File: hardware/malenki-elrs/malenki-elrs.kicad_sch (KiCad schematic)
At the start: 36 parts, among them J1 Conn_01x02_Male-Connector, J2 PROG Header, J3 Weapons, U1 SPX3819M5-L-3-3, U7 ESP32-S3FN8, Y1 ECS-400-10-37B2-CKY-TR

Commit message: Generated production files
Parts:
- C1, C14, C5: LCSC C96446 -> (none); LCSC Part # (none) -> C96446; Manufacturer Samsung -> (none)
- C10, C11, C13, C4, C7, C9: LCSC C1525 -> (none); LCSC Part # (none) -> C1525
- C12, C15, C8: LCSC C52923 -> (none); LCSC Part # (none) -> C52923
- C2, C3: LCSC C1547 -> (none); LCSC Part # (none) -> C1547
- C6: LCSC C15195 -> (none); LCSC Part # (none) -> C15195
- D2: LCSC C25503345 -> (none); LCSC Part # (none) -> C25503345; Manufacturer XINGLIGHT -> (none)
- L4: LCSC C76884 -> (none); LCSC Part # (none) -> C76884
- R1, R13, R2, R6, R8: LCSC C25744 -> (none); LCSC Part # (none) -> C25744
- R10, R11, R12, R14, R3, R4, R5: LCSC C25117 -> (none); LCSC Part # (none) -> C25117
- R7: LCSC C25779 -> (none); LCSC Part # (none) -> C25779
- U1: LCSC C9055 -> (none); LCSC Part # (none) -> C9055
- U2: renamed from U7; LCSC C2913196 -> (none); LCSC Part # (none) -> C2913196
- Y1: LCSC C5371760 -> (none); LCSC Part # (none) -> C5371760
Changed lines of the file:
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@@
 			)
 		)
-		(property "LCSC" "C25117"
-			(at 210.82 76.2 0)
-			(hide yes)
-			(show_name no)
-			(do_not_autoplace no)
-			(effects
-				(font
-					(size 1.27 1.27)
-				)
-			)
-		)
-		(property "Manufacturer" ""
+		(property "LCSC Part #" "C25117"
 			(at 210.82 76.2 0)
 			(hide yes)
@@
 			)
 		)
-		(property "LCSC" "C25744"
-			(at 53.34 123.19 0)
-			(hide yes)
-			(show_name no)
-			(do_not_autoplace no)
-			(effects
-				(font
-					(size 1.27 1.27)
-				)
-			)
-		)
-		(property "Manufacturer" ""
+		(property "LCSC Part #" "C25744"
 			(at 53.34 123.19 0)
 			(hide yes)
@@
 			)
 		)
-		(property "LCSC" "C1525"
+		(property "LCSC Part #" "C1525"
 			(at 212.09 95.25 0)
 			(hide yes)
@@
 			)
 		)
-		(property "LCSC" "C25503345"
+		(property "LCSC Part #" "C25503345"
 			(at 163.83 181.61 0)
 			(hide yes)
@@
 			)
 		)
-		(property "Manufacturer" "XINGLIGHT"
-			(at 163.83 181.61 0)
-			(hide yes)
-			(show_name no)
-			(do_not_autoplace no)
-			(effects
-				(font
-					(size 1.27 1.27)
-				)
-			)
-		)
 		(property "Sim.Pins" "1=K 2=A"
 			(at 163.83 181.61 0)
@@
 			)
 		)
-		(property "LCSC" "C25117"
+		(property "LCSC Part #" "C25117"
 			(at 30.48 72.39 0)
 			(hide yes)
@@
 			)
 		)
-		(property "LCSC" "C52923"
+		(property "LCSC Part #" "C52923"
 			(at 54.61 54.61 0)
 			(hide yes)
@@
 			)
 		)
-		(property "LCSC" "C1547"
+		(property "LCSC Part #" "C1547"
 			(at 106.68 181.61 0)
 			(hide yes)
@@
 			)
 		)
-		(property "LCSC" "C25117"
-			(at 163.83 173.99 0)
-			(hide yes)
-			(show_name no)
-			(do_not_autoplace no)
-			(effects
-				(font
-					(size 1.27 1.27)
-				)
-			)
-		)
-		(property "Manufacturer" ""
+		(property "LCSC Part #" "C25117"
 			(at 163.83 173.99 0)
 			(hide yes)
@@
 		(dnp no)
 		(fields_autoplaced yes)
-		(property "Reference" "U7"
+		(property "Reference" "U2"
 			(at 140.97 48.26 0)
 			(show_name no)
@@
 			)
 		)
-		(property "LCSC" "C2913196"
+		(property "LCSC Part #" "C2913196"
 			(at 107.95 58.42 0)
 			(hide yes)
@@
 			(project "malenki-elrs"
 				(path "/f41619e3-8cf2-4511-8a51-762d4de43197"
-					(reference "U7")
+					(reference "U2")
 					(unit 1)
 				)
@@
 			)
 		)
-		(property "LCSC" "C1525"
+		(property "LCSC Part #" "C1525"
 			(at 77.47 54.61 0)
 			(hide yes)
@@
 			)
 		)
-		(property "LCSC" "C76884"
+		(property "LCSC Part #" "C76884"
 			(at 71.12 49.53 90)
 			(hide yes)
@@
 			)
 		)
-		(property "LCSC" "C25117"
+		(property "LCSC Part #" "C25117"
 			(at 67.31 116.84 0)
 			(hide yes)
@@
 			)
 		)
-		(property "LCSC" "C52923"
+		(property "LCSC Part #" "C52923"
 			(at 207.01 54.61 0)
 			(hide yes)
@@
 			)
 		)
-		(property "LCSC" "C1547"
+		(property "LCSC Part #" "C1547"
 			(at 88.9 181.61 0)
 			(hide yes)
@@
 			)
 		)
-		(property "LCSC" "C1525"
+		(property "LCSC Part #" "C1525"
 			(at 64.77 54.61 0)
 			(hide yes)
@@
 			)
 		)
-		(property "LCSC" "C25117"
-			(at 210.82 83.82 0)
-			(hide yes)
-			(show_name no)
-			(do_not_autoplace no)
-			(effects
-				(font
-					(size 1.27 1.27)
-				)
-			)
-		)
-		(property "Manufacturer" ""
+		(property "LCSC Part #" "C25117"
 			(at 210.82 83.82 0)
 			(hide yes)
@@
 			)
 		)
-		(property "LCSC" "C9055"
+		(property "LCSC Part #" "C9055"
 			(at 83.82 30.48 0)
 			(hide yes)
@@
 			)
 		)
-		(property "LCSC" "C1525"
+		(property "LCSC Part #" "C1525"
 			(at 36.83 78.74 0)
 			(hide yes)
@@
 			)
 		)
-		(property "LCSC" "C52923"
+		(property "LCSC Part #" "C52923"
 			(at 191.77 133.35 0)
 			(hide yes)
@@
 			)
 		)
-		(property "LCSC" "C25744"
-			(at 55.88 123.19 0)
-			(hide yes)
-			(show_name no)
-			(do_not_autoplace no)
-			(effects
-				(font
-					(size 1.27 1.27)
-				)
-			)
-		)
-		(property "Manufacturer" ""
+		(property "LCSC Part #" "C25744"
 			(at 55.88 123.19 0)
 			(hide yes)
@@
 			)
 		)
-		(property "LCSC" "C96446"
-			(at 43.18 54.61 0)
-			(hide yes)
-			(show_name no)
-			(do_not_autoplace no)
-			(effects
-				(font
-					(size 1.27 1.27)
-				)
-			)
-		)
-		(property "Manufacturer" "Samsung"
+		(property "LCSC Part #" "C96446"
 			(at 43.18 54.61 0)
 			(hide yes)
@@
 			)
 		)
-		(property "LCSC" "C25117"
+		(property "LCSC Part #" "C25117"
 			(at 67.31 107.95 0)
 			(hide yes)
@@
 			)
 		)
-		(property "LCSC" "C5371760"
+		(property "LCSC Part #" "C5371760"
 			(at 97.79 176.53 0)
 			(hide yes)
@@
 			)
 		)
-		(property "LCSC" "C25779"
-			(at 132.08 173.99 0)
-			(hide yes)
-			(show_name no)
-			(do_not_autoplace no)
-			(effects
-				(font
-					(size 1.27 1.27)
-				)
-			)
-		)
-		(property "Manufacturer" ""
+		(property "LCSC Part #" "C25779"
 			(at 132.08 173.99 0)
 			(hide yes)
@@
 			)
 		)
-		(property "LCSC" "C96446"
-			(at 104.14 29.21 0)
-			(hide yes)
-			(show_name no)
-			(do_not_autoplace no)
-			(effects
-				(font
-					(size 1.27 1.27)
-				)
-			)
-		)
-		(property "Manufacturer" "Samsung"
+		(property "LCSC Part #" "C96446"
 			(at 104.14 29.21 0)
 			(hide yes)
@@
 			)
 		)
-		(property "LCSC" "C96446"
-			(at 59.69 29.21 0)
-			(hide yes)
-			(show_name no)
-			(do_not_autoplace no)
-			(effects
-				(font
-					(size 1.27 1.27)
-				)
-			)
-		)
-		(property "Manufacturer" "Samsung"
+		(property "LCSC Part #" "C96446"
 			(at 59.69 29.21 0)
 			(hide yes)
@@
 			)
 		)
-		(property "LCSC" "C25744"
+		(property "LCSC Part #" "C25744"
 			(at 55.88 91.44 0)
 			(hide yes)
@@
 			)
 		)
-		(property "LCSC" "C25117"
-			(at 49.53 97.79 0)
-			(hide yes)
-			(show_name no)
-			(do_not_autoplace no)
-			(effects
-				(font
-					(size 1.27 1.27)
-				)
-			)
-		)
-		(property "Manufacturer" ""
+		(property "LCSC Part #" "C25117"
 			(at 49.53 97.79 0)
 			(hide yes)
@@
 			)
 		)
-		(property "LCSC" "C1525"
+		(property "LCSC Part #" "C1525"
 			(at 179.07 133.35 0)
 			(hide yes)
@@
 			)
 		)
-		(property "LCSC" "C1525"
+		(property "LCSC Part #" "C1525"
 			(at 83.82 99.06 0)
 			(hide yes)
@@
 			)
 		)
-		(property "LCSC" "C25744"
-			(at 132.08 182.88 0)
-			(hide yes)
-			(show_name no)
-			(do_not_autoplace no)
-			(effects
-				(font
-					(size 1.27 1.27)
-				)
-			)
-		)
-		(property "Manufacturer" ""
+		(property "LCSC Part #" "C25744"
 			(at 132.08 182.88 0)
 			(hide yes)
@@
 			)
 		)
-		(property "LCSC" "C15195"
+		(property "LCSC Part #" "C15195"
 			(at 194.31 54.61 0)
 			(hide yes)
@@
 			)
 		)
-		(property "LCSC" "C25744"
+		(property "LCSC Part #" "C25744"
 			(at 36.83 66.04 0)
 			(hide yes)

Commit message: Updated production files
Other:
- note added: "Must be pulled low at boot (using weak internal pull down)"
- note removed: "Must be pulled low at boot"
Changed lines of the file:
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@@
 		)
 	)
-	(text "Must be pulled low at boot"
+	(text "Must be pulled low at boot (using weak internal pull down)"
 		(exclude_from_sim no)
-		(at 188.468 73.914 0)
+		(at 204.47 73.914 0)
 		(effects
 			(font
@@
 		)
 	)
-	(text "Must be pulled low at boot"
+	(text "Must be pulled low at boot (using weak internal pull down)"
 		(exclude_from_sim no)
-		(at 188.468 71.374 0)
+		(at 204.47 71.374 0)
 		(effects
 			(font

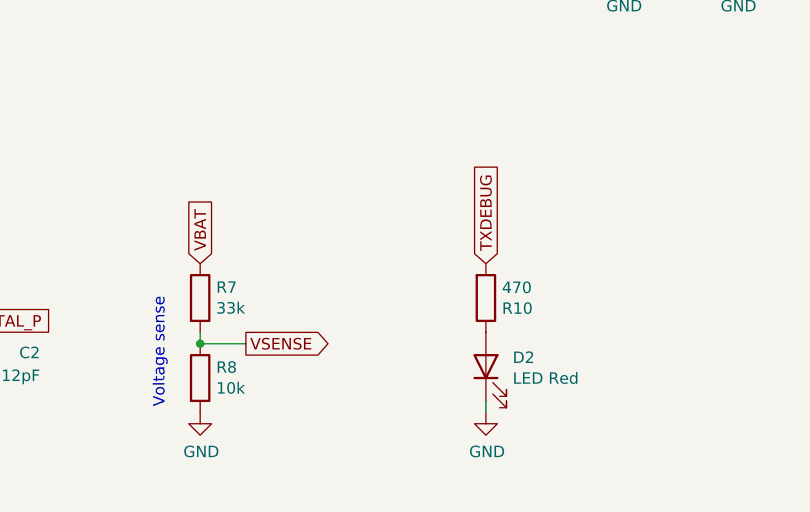
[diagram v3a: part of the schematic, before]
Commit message: Added power led, and images
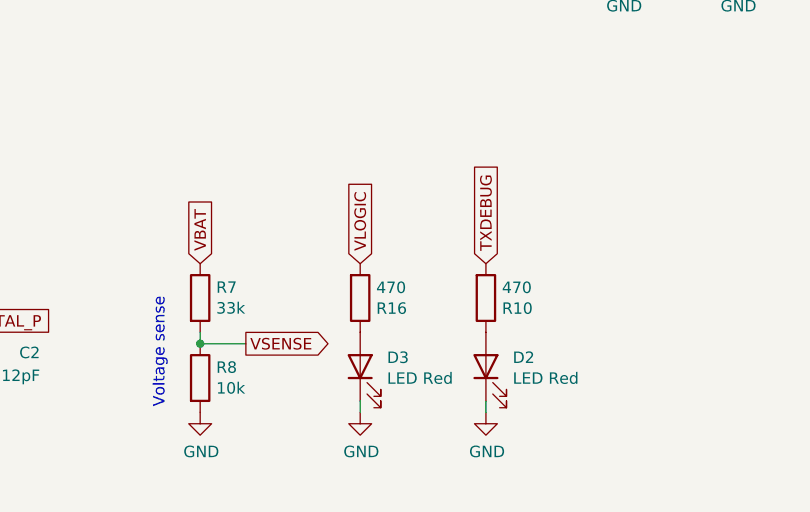
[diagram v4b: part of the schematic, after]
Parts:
- added D3: LED Red, LED_SMD:LED_0402_1005Metric, symbol Device:LED
- added R16: 470, Resistor_SMD:R_0402_1005Metric, symbol malenki-nano-rescue:R-Device
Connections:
- net GND: now also D3.1 (K)
- net VLOGIC: now also R16.2
- new net: D3.2 (A), R16.1
